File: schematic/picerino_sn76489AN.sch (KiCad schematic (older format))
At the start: 23 parts, among them CON1 PICERINO-EDGE, J1 Conn_01x02, J2 Conn_01x02, J3 Conn_01x02, U1 sn76489an, U2 74LS00, U3 LM386, Y1 3.579545Mhz

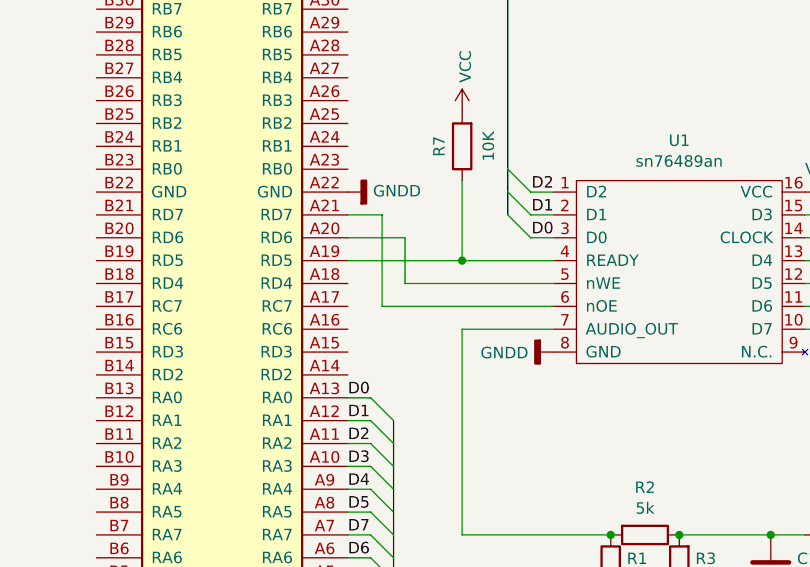
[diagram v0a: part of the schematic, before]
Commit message: updated kicad schematic and pcb so ready is tied to RC7
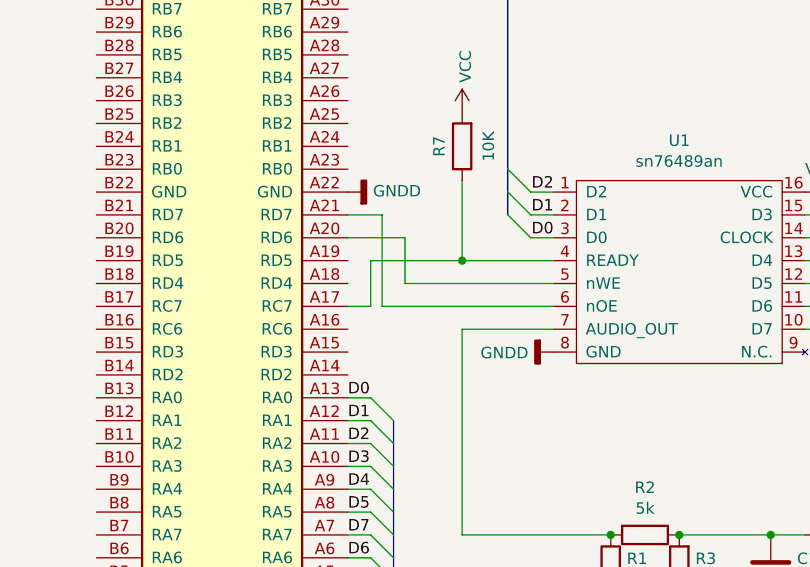
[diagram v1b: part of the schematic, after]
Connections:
- net at R7.1, U1.4 (READY): now also CON1.A17 (RC7); no longer CON1.A19 (RD5)
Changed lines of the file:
@@
 	3250 3700 3900 3700
-Wire Wire Line
-	3500 3600 3000 3600
-Connection ~ 3500 3600
 Wire Wire Line
 	3250 3500 3250 3700
@@
 Wire Bus Line
 	3200 5750 1450 5750
+Wire Wire Line
+	3000 3800 3100 3800
+Wire Wire Line
+	3100 3800 3100 3600
+Wire Wire Line
+	3100 3600 3500 3600
 Wire Bus Line
 	3700 1800 3700 3400
@@
 Wire Bus Line
 	3200 4300 3200 5750
+Connection ~ 3500 3600
 $EndSCHEMATC

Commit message: reverse bit order on pcb to remove software reversal
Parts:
- U1: symbol Vintage_PC_Audio:sn76489an -> picerino_sn76489AN-rescue:sn76489an-Vintage_PC_Audio
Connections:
- net D0: now also CON1.A7 (RA7); no longer CON1.A13 (RA0)
- net D1: now also CON1.A6 (RA6); no longer CON1.A12 (RA1)
- net D2: now also CON1.A8 (RA5); no longer CON1.A11 (RA2)
- net D3: now also CON1.A9 (RA4); no longer CON1.A10 (RA3)
- net D4: now also CON1.A10 (RA3); no longer CON1.A9 (RA4)
- net D5: now also CON1.A11 (RA2); no longer CON1.A8 (RA5)
- net D6: now also CON1.A12 (RA1); no longer CON1.A6 (RA6)
- net D7: now also CON1.A13 (RA0); no longer CON1.A7 (RA7)
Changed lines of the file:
@@
 $EndComp
 $Comp
-L Vintage_PC_Audio:sn76489an U1
+L picerino_sn76489AN-rescue:sn76489an-Vintage_PC_Audio U1
 U 1 1 61DA60DE
 P 4450 3400
@@
 	1    0    0    -1
 $EndComp
+Text Label 3000 4500 0    50   ~ 0
+D4
 Text Label 3000 4600 0    50   ~ 0
-D4
-Text Label 3000 4500 0    50   ~ 0
 D3
+Text Label 3000 4700 0    50   ~ 0
+D2
 Text Label 3000 4400 0    50   ~ 0
-D2
-Text Label 3000 4700 0    50   ~ 0
 D5
+Text Label 3000 4900 0    50   ~ 0
+D1
 Text Label 3000 4300 0    50   ~ 0
-D1
-Text Label 3000 4900 0    50   ~ 0
 D6
+Text Label 3000 4200 0    50   ~ 0
+D7
 Text Label 3000 4800 0    50   ~ 0
-D7
-Text Label 3000 4200 0    50   ~ 0
 D0
 $Comp
@@
 Wire Wire Line
 	3100 3600 3500 3600
+Connection ~ 3500 3600
 Wire Bus Line
 	3700 1800 3700 3400
@@
 Wire Bus Line
 	3200 4300 3200 5750
-Connection ~ 3500 3600
 $EndSCHEMATC

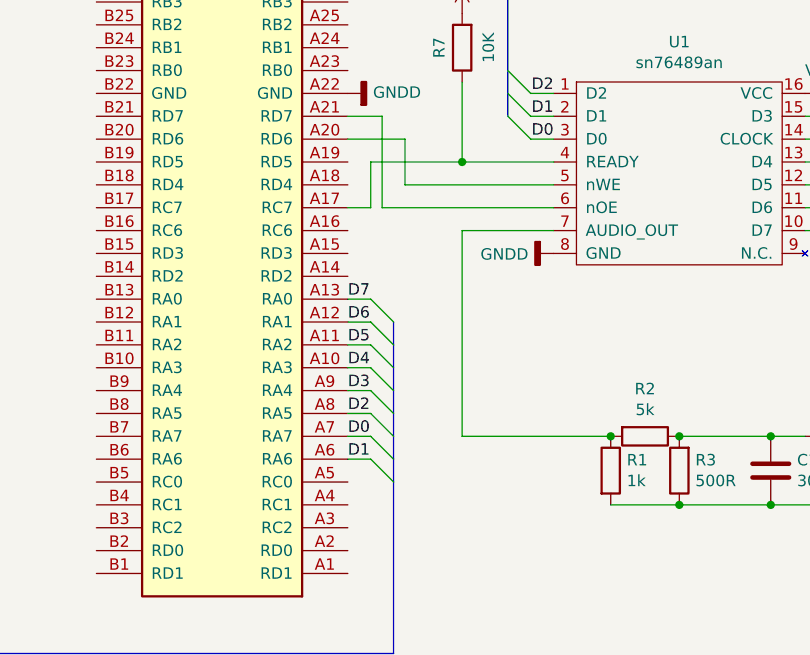
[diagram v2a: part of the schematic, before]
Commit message: fixed pcb so bits are reversed as they should be
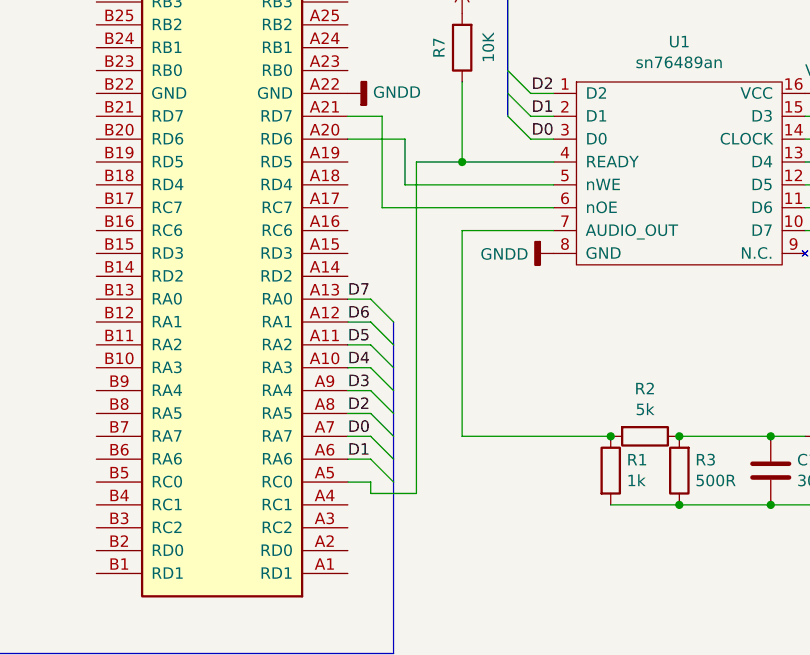
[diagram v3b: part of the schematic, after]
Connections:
- net at R7.1, U1.4 (READY): now also CON1.A5 (RC0); no longer CON1.A17 (RC7)
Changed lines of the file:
@@
 	3200 5750 1450 5750
 Wire Wire Line
-	3000 3800 3100 3800
+	3500 3600 3300 3600
+Connection ~ 3500 3600
 Wire Wire Line
-	3100 3800 3100 3600
+	3300 5050 3100 5050
 Wire Wire Line
-	3100 3600 3500 3600
-Connection ~ 3500 3600
+	3100 5050 3100 5000
+Wire Wire Line
+	3100 5000 3000 5000
+Wire Wire Line
+	3300 3600 3300 5050
 Wire Bus Line
 	3700 1800 3700 3400
